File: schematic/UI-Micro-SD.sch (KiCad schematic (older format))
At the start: 31 parts, among them IC1 TCA9534PWR, J1 Conn_02x08_Odd_Even, J2 Conn_02x08_Odd_Even, J6 Conn_01x08, J8 Solder-Jumper-3-3-3-Open, Q1 BSS138, U1 SFV14R-2STE1HLF, U2 DizzyBITLogo, U3 DizzyBIT-Layout

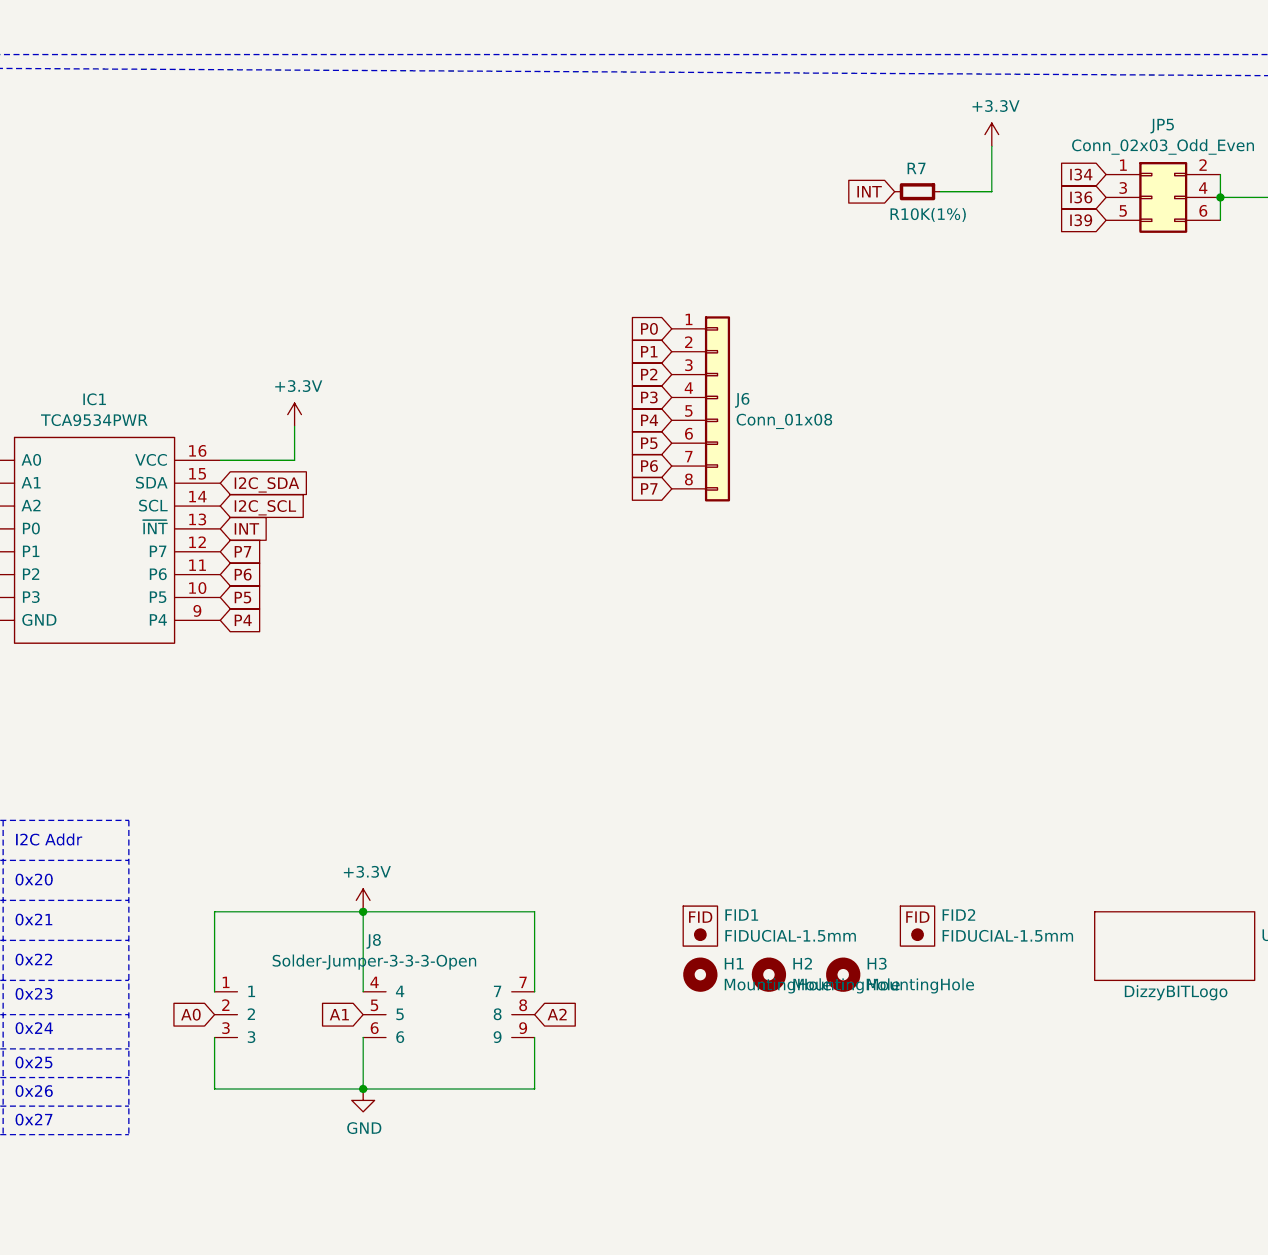
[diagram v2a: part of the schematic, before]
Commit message: Designed tracks and silk labels
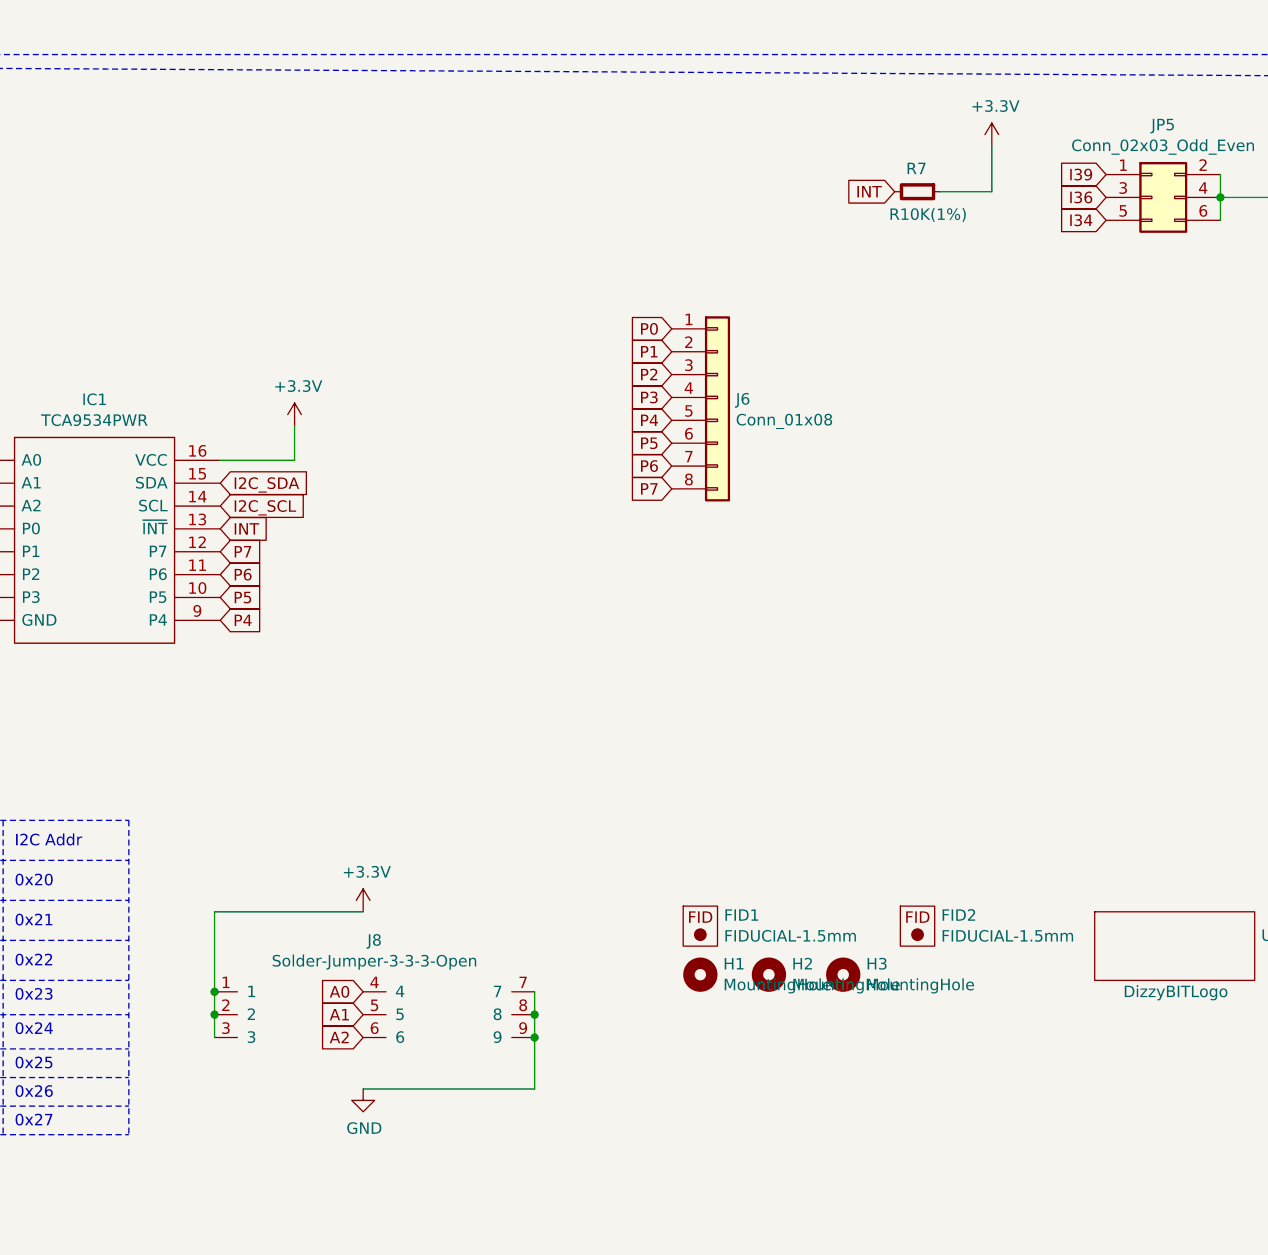
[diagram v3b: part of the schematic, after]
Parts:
- SD1: footprint Connfly:DS-1139-04 -> Connfly:DS1139-05
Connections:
- net +3V3: now also J8.2, J8.3; no longer J8.4, J8.7
- net A0: now also J8.4; no longer J8.2
- net A2: now also J8.6; no longer J8.8
- net GND: now also J8.7, J8.8; no longer J8.3, J8.6
- net I34: now also JP5.5 (Pin_5); no longer JP5.1 (Pin_1)
- net I39: now also JP5.1 (Pin_1); no longer JP5.5 (Pin_5)
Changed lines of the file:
@@
 F 0 "SD1" H 3200 1990 50  0000 C CNN
 F 1 "47309-3351" H 3200 1899 50  0000 C CNN
-F 2 "Connfly:DS-1139-04" H 3700 1825 50  0001 L CNN
+F 2 "Connfly:DS1139-05" H 3700 1825 50  0001 L CNN
 F 3 "https://componentsearchengine.com/Datasheets/1/47309-3351.pdf" H 3700 1725 50  0001 L CNN
 F 4 "WM10795DKR-ND" H 2550 1725 50  0001 C CNN "dk_pn"
@@
 Wire Wire Line
 	8975 8950 8975 8800
-Text GLabel 10050 10525 0    50   Input ~ 0
+Text GLabel 10700 10425 0    50   Input ~ 0
 A0
 $Comp
@@
 Text GLabel 10700 10525 0    50   Input ~ 0
 A1
-Text GLabel 11450 10525 2    50   Input ~ 0
+Text GLabel 10700 10625 0    50   Input ~ 0
 A2
 Text Notes 7525 9800 0    50   ~ 0
@@
 Wire Wire Line
 	10050 10075 10700 10075
-Wire Wire Line
-	10700 10425 10700 10075
-Connection ~ 10700 10075
-Wire Wire Line
-	10700 10075 11450 10075
-Wire Wire Line
-	11450 10075 11450 10425
 $Comp
 L power:GND #PWR0119
@@
 $EndComp
 Wire Wire Line
-	10050 10625 10050 10850
-Wire Wire Line
-	10050 10850 10700 10850
-Wire Wire Line
-	10700 10625 10700 10850
-Connection ~ 10700 10850
-Wire Wire Line
 	11450 10625 11450 10850
 Wire Wire Line
@@
 Wire Wire Line
 	14450 6950 14450 7050
-Text GLabel 13950 6850 0    50   Input ~ 0
+Text GLabel 13950 7050 0    50   Input ~ 0
 I34
 Text GLabel 13950 6950 0    50   Input ~ 0
 I36
-Text GLabel 13950 7050 0    50   Input ~ 0
+Text GLabel 13950 6850 0    50   Input ~ 0
 I39
 $Comp
@@
 	7875 4300 7875 4950
 NoConn ~ 8425 4500
+Wire Wire Line
+	11450 10425 11450 10525
+Connection ~ 11450 10625
+Connection ~ 11450 10525
+Wire Wire Line
+	11450 10525 11450 10625
+Wire Wire Line
+	10050 10425 10050 10525
+Connection ~ 10050 10425
+Connection ~ 10050 10525
+Wire Wire Line
+	10050 10525 10050 10625
 $EndSCHEMATC
